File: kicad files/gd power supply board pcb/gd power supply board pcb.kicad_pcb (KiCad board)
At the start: 2 copper layers, 166.1 x 47.2 mm, 114 parts, among them J1 15V_IN, J2 15V_IN, J3 Edge Connector, Q1 FDS9435A, Q2 BC817, Q3 MMBT3906, Q4 FDS9435A, U1 MAX17580, U2 mc34063, U3 TPS563240DDCR, U4 TPS563240DDCR

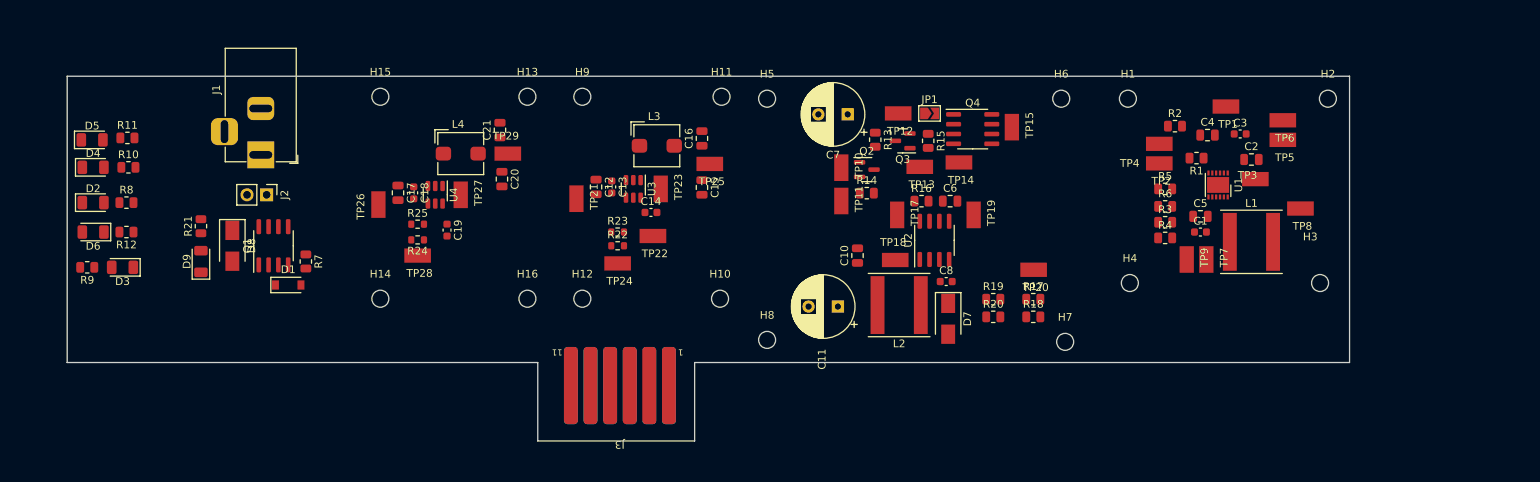
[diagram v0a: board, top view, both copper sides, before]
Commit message: minor fixes and compacting the floorplan. stacked 5V supplies for maximum minimage.
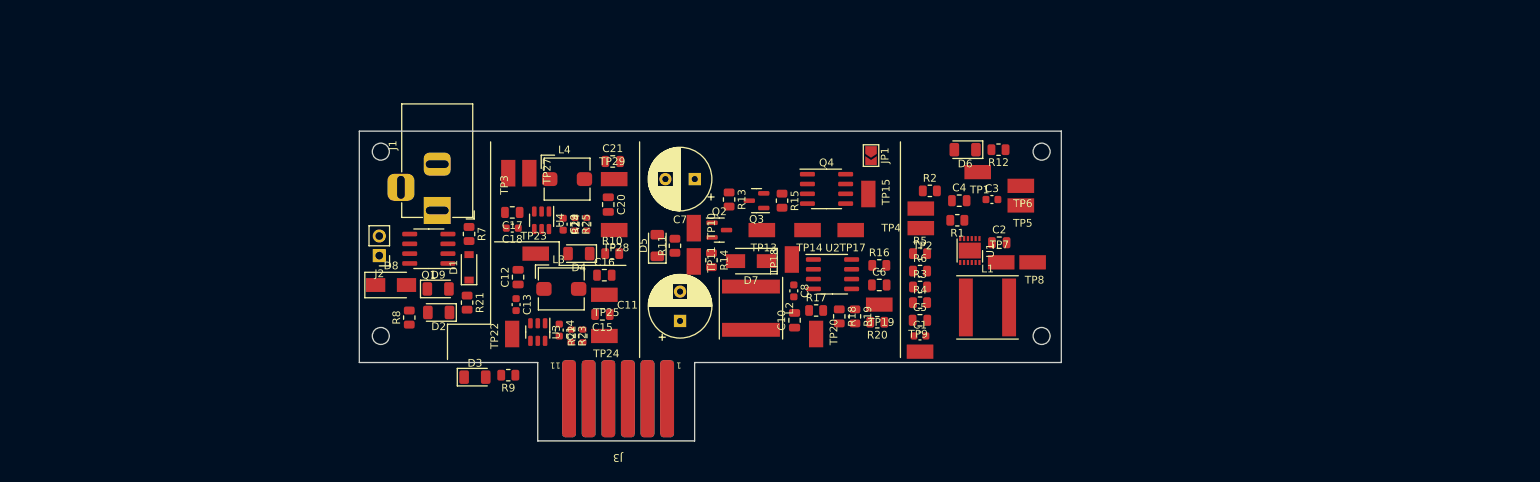
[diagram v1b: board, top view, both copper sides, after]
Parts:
- removed H10, H11, H12, H13, H14, H15, H16, H5, H6, H7, H8, H9: MountingHole, MountingHole:MountingHole_2.2mm_M2
- removed TP12, TP21, TP26: TestPoint_Harwin, My Libraries:Harwin-S1751-46-Test-Point
- moved R12 113.5 mm to (182.4, 81.3)
- moved D6 113.5 mm to (178.1, 81.3)
- moved H4 97.3 mm to (102.4, 105.4)
- moved H1 97.0 mm to (102.4, 81.5)
- moved TP3 96.8 mm to (118.9, 84.3), turned to 90 degrees
- moved D5 74.5 mm to (138.2, 93.7), turned to 90 degrees
- moved R11 72.3 mm to (140.5, 93.7), turned to 90 degrees
- moved D4 63.9 mm to (128.0, 94.7), turned to 180 degrees
- moved R10 63.7 mm to (132.3, 94.7)
- moved R9 56.3 mm to (118.9, 110.5)
- moved D3 47.8 mm to (114.6, 110.7), turned to 0 degrees
- moved D2 47.0 mm to (109.9, 102.4), turned to 180 degrees
- moved R8 39.5 mm to (106.0, 103.0), turned to 90 degrees
- moved C1 38.7 mm to (172.2, 105.4)
- moved C5 38.7 mm to (172.2, 103.4)
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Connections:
- R8 pad 2: /15v_In -> /15v_Raw
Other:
- board size 166.1 x 47.2 mm -> 90.9 x 40.1 mm

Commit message: pre-routing try 1
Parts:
- removed R4: 0, Resistor_SMD:R_0805_2012Metric
- removed R6: 1k, Resistor_SMD:R_0805_2012Metric
- removed TP1, TP2, TP4: TestPoint_Harwin, My Libraries:Harwin-S1751-46-Test-Point
- added C9: 1u, Capacitor_SMD:C_0805_2012Metric, B.Cu at (178.3, 92.4)
- added JP2: 15V_byp, Jumper:SolderJumper-2_P1.3mm_Open_TrianglePad1.0x1.5mm, F.Cu at (114.8, 100.6)
- added JP3: neg_12_jmp, Jumper:SolderJumper-2_P1.3mm_Open_TrianglePad1.0x1.5mm, F.Cu at (179.7, 81.0)
- added JP4: mega_5v_jmp, Jumper:SolderJumper-2_P1.3mm_Open_TrianglePad1.0x1.5mm, F.Cu at (118.1, 98.9)
- added JP5: stb_5v_jmp, Jumper:SolderJumper-2_P1.3mm_Open_TrianglePad1.0x1.5mm, F.Cu at (118.4, 82.2)
- C4: footprint Capacitor_SMD:C_0805_2012Metric -> Capacitor_SMD:C_0603_1608Metric
- R1: footprint Resistor_SMD:R_0805_2012Metric -> Resistor_SMD:R_0402_1005Metric
- TP5, TP6, TP8: footprint My Libraries:Harwin-S1751-46-Test-Point -> TestPoint:TestPoint_Pad_1.0x1.0mm
- moved R12 26.5 mm to (175.4, 106.9), turned to 90 degrees
- moved D6 26.1 mm to (179.0, 107.4), turned to 0 degrees
- moved C7 19.9 mm to (162.9, 84.3), turned to -90 degrees
- moved C1 19.2 mm to (176.7, 86.8), turned to 180 degrees
- moved TP20 18.8 mm to (143.4, 94.3)
- moved TP8 15.4 mm to (171.9, 92.2)
- moved TP14 15.0 mm to (144.2, 85.0), turned to 90 degrees
- moved C5 11.4 mm to (180.9, 96.0), turned to 90 degrees
- moved J3 9.93 mm to (143.0, 118.6)
- moved TP5 9.64 mm to (177.1, 83.4), turned to 180 degrees
- moved C10 9.58 mm to (146.7, 100.9), turned to -90 degrees
- moved TP15 9.44 mm to (156.5, 84.3), turned to 180 degrees
- moved R14 8.89 mm to (140.2, 88.2), turned to 180 degrees
- moved R2 8.84 mm to (181.9, 89.4), turned to -90 degrees
- moved JP1 8.68 mm to (157.2, 81.2)
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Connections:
- C12 pad 1: /Vin -> Net-(C12-Pad1)
- C13 pad 1: /Vin -> Net-(C12-Pad1)
- C17 pad 1: /Vin -> /stb_5v/stb_Vin
- C18 pad 1: /Vin -> /stb_5v/stb_Vin
- C2 pad 1: /Vin -> /neg12/neg12_Vin
- J3 pad 5: /stb_5v -> /mega_5v
- J3 pad 7: /mega_5v -> /stb_5v
- R3 pad 2: Net-(R3-Pad2) -> /neg12/FB
- R5 pad 2: Net-(R5-Pad2) -> /Neg12_Out
- U1 pad 1: /Vin -> /neg12/neg12_Vin
- U3 pad 3: /Vin -> Net-(C12-Pad1)
- U4 pad 3: /Vin -> /stb_5v/stb_Vin
- U4 pad 5: /Vin -> /stb_5v/stb_Vin
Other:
- board size 90.9 x 40.1 mm -> 86.9 x 40.1 mm

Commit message: 0 unrouted - drc pass - need to clean silks
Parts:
- JP2: moved to B.Cu
- moved D6 12.7 mm to (185.2, 96.3), turned to 90 degrees
- moved JP2 11.9 mm to (114.6, 88.6), turned to 0 degrees
- moved R12 11.2 mm to (183.0, 98.6), turned to -90 degrees
- moved TP18 6.85 mm to (154.6, 92.4), turned to 0 degrees
- moved TP7 6.52 mm to (175.5, 104.0), turned to 180 degrees
- moved TP19 5.24 mm to (163.3, 105.5)
- moved C11 3.51 mm to (143.0, 100.8), turned to 180 degrees
- moved C9 2.95 mm to (177.1, 89.7), turned to 180 degrees
- moved C10 1.88 mm to (146.8, 102.7)
- moved C5 1.72 mm to (182.3, 95.0), turned to 180 degrees
- moved C7 1.39 mm to (162.6, 85.6), turned to 0 degrees
- moved R2 1.04 mm to (182.9, 89.4)
- moved TP6 1.04 mm to (185.0, 88.7)
- moved C13 0.89 mm to (119.9, 101.4), turned to 180 degrees
- moved R20 0.81 mm to (164.3, 102.5)
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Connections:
- J3 pad 11: /Analog_En -> /Mega_En
- J3 pad 12: /Mega_En -> /Analog_En
- J3 pad 5: /mega_5v -> /stb_5v
- J3 pad 7: /stb_5v -> /mega_5v
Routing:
- net /Analog_En: track 0.00 -> 179.7 mm, vias 0 -> 4
- net /Mega_En: track 0.00 -> 29.3 mm, vias 0 -> 2
- net /mega_5v: track 0.00 -> 20.5 mm, vias 0 -> 2
- net Net-(R18-Pad1): track 0.00 -> 13.7 mm, vias 0 -> 2
- net Net-(R24-Pad1): track 0.00 -> 7.42 mm
- net /neg12/~{RESET}: track 0.00 -> 6.92 mm
- net /Pos12_Out: track 0.00 -> 6.64 mm
- net Net-(C8-Pad1): track 0.00 -> 4.86 mm
- net Net-(C3-Pad1): track 0.00 -> 4.11 mm
- net /stb_5v/stb_Vin: track 0.00 -> 3.76 mm, vias 0 -> 2
- net GND: track 0.00 -> 3.06 mm, vias 0 -> 32
- net Net-(D3-Pad2): track 0.00 -> 2.85 mm
- net Net-(R19-Pad2): track 0.00 -> 2.84 mm
- net Net-(C4-Pad1): track 0.00 -> 2.55 mm
- net Net-(D5-Pad2): track 0.00 -> 2.45 mm
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- added copper zone on B.Cu, net /15v_Raw
- added copper zone on F.Cu, net /15v_Raw
- added copper zone on F.Cu, net /Neg12_Out
- added copper zone on F.Cu, net /Pos12_Out
- added copper zone on F.Cu, net /Vin
- added copper zone on F.Cu, net /mega_5v
- added copper zone on F.Cu, net /neg12/FB
- added copper zone on F.Cu, net /neg12/neg12_Vin
- added copper zone on F.Cu, net /pos12/15V_SW
- added copper zone on F.Cu, net /pos12/Isense
- added copper zone on F.Cu, net /pos12/SW
- added copper zone on F.Cu, net /stb_5v
- added copper zone on F.Cu, net /stb_5v/stb_Vin
- added copper zone on B.Cu, net GND
- added copper zone on F.Cu, net GND
- added copper zone on F.Cu, net Net-(C12-Pad1)
- added copper zone on B.Cu, net Net-(C14-Pad1)
- added copper zone on F.Cu, net Net-(C14-Pad1)
- added copper zone on F.Cu, net Net-(C14-Pad2)
- added copper zone on B.Cu, net Net-(C19-Pad1)
- added copper zone on F.Cu, net Net-(C19-Pad1)
- added copper zone on F.Cu, net Net-(C19-Pad2)
- added copper zone on F.Cu, net Net-(C4-Pad2)
- added copper zone on F.Cu, net Net-(D1-Pad2)
- added copper zone on F.Cu, net Net-(D2-Pad2)
- added copper zone on F.Cu, net Net-(D8-Pad2)
- added copper zone on F.Cu, net Net-(D9-Pad2)
- added copper zone on F.Cu, net Net-(Q2-Pad2)
- added copper zone on F.Cu, net Net-(Q2-Pad3)
- added copper zone on F.Cu, net Net-(Q3-Pad1)
- added copper zone on F.Cu, net Net-(R22-Pad1)
- added copper zone on F.Cu, net Net-(R24-Pad1)
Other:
- outline, holes or cut-outs redrawn

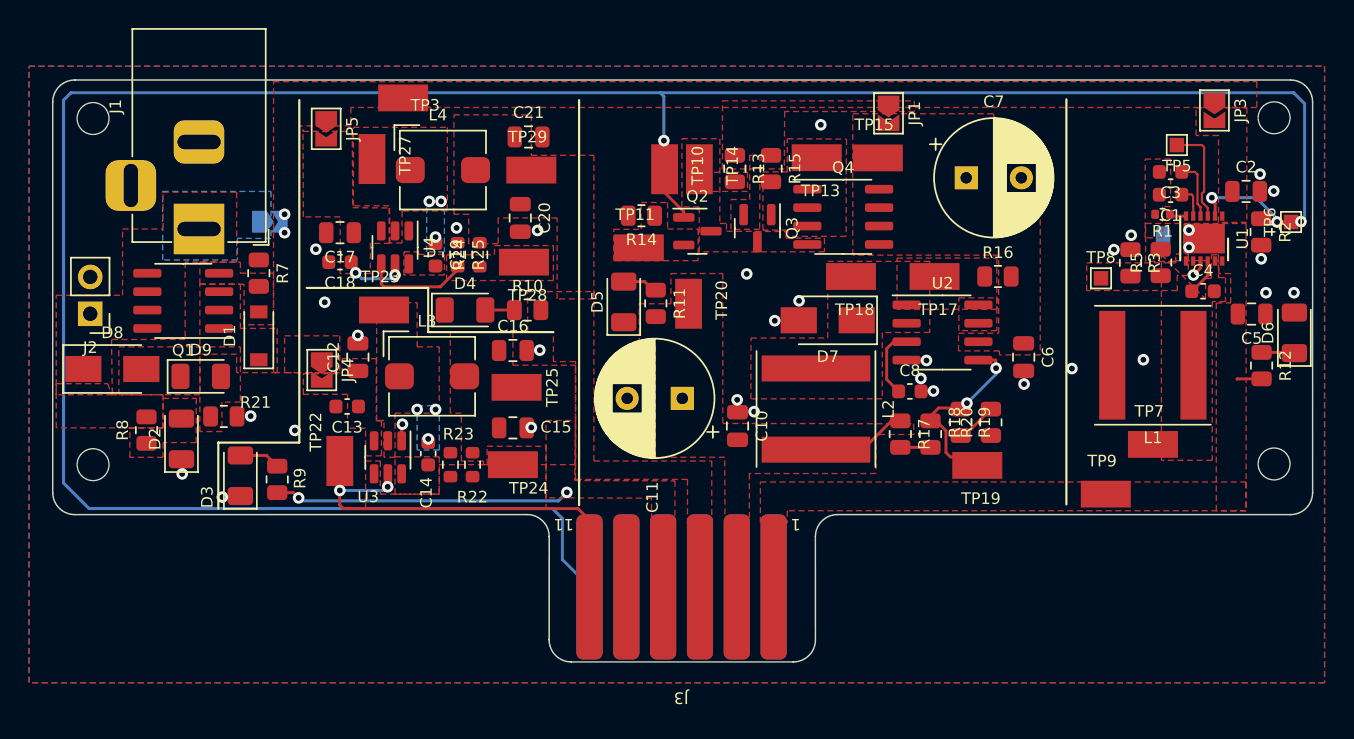
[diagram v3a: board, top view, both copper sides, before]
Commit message: cleaned up silks. minor fixes
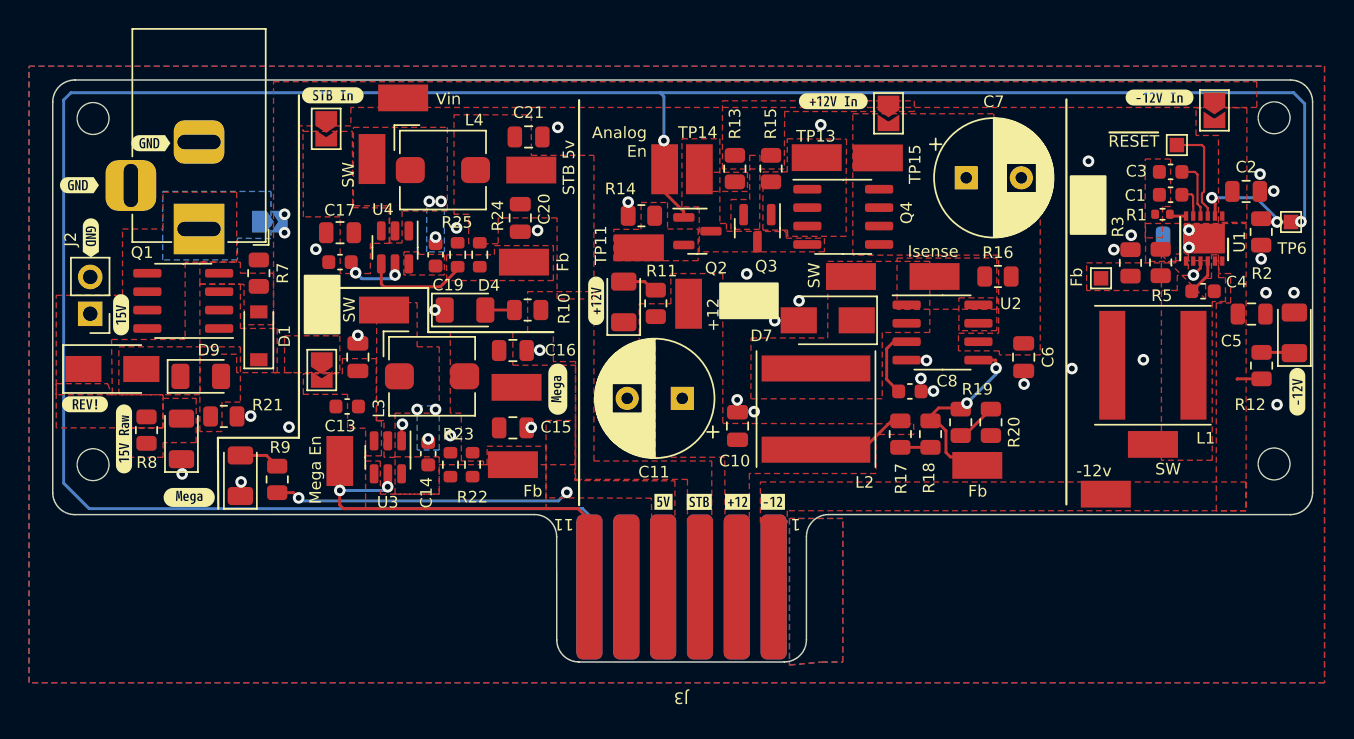
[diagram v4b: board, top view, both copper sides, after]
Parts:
- added TP1: TestPoint_Harwin, My Libraries:Harwin-S1751-46-Test-Point, F.Cu at (171.0, 87.5)
- added TP2: TestPoint_Harwin, My Libraries:Harwin-S1751-46-Test-Point, F.Cu at (118.2, 94.3)
- added TP4: TestPoint_Harwin, My Libraries:Harwin-S1751-46-Test-Point, F.Cu at (147.7, 94.0)
- added kibuzzard-62380C70: G***, kibuzzard-62380C70, F.Cu at (104.5, 103.6)
- added kibuzzard-62380CC4: G***, kibuzzard-62380CC4, F.Cu at (101.8, 101.2)
- added kibuzzard-62380CD9: G***, kibuzzard-62380CD9, F.Cu at (109.0, 107.7)
- added kibuzzard-62380CD9: G***, kibuzzard-62380CD9, F.Cu at (134.4, 100.2)
- added kibuzzard-62380D7E: G***, kibuzzard-62380D7E, F.Cu at (118.9, 79.9)
- added kibuzzard-62380DAB: G***, kibuzzard-62380DAB, F.Cu at (104.3, 95.1)
- added kibuzzard-62380E7D: G***, kibuzzard-62380E7D, F.Cu at (137.1, 94.1)
- added kibuzzard-62380F2D: G***, kibuzzard-62380F2D, F.Cu at (153.4, 80.3)
- added kibuzzard-62380F77: G***, kibuzzard-62380F77, F.Cu at (185.4, 100.4)
- added kibuzzard-62380FA1: G***, kibuzzard-62380FA1, F.Cu at (175.9, 80.1)
- added kibuzzard-62380FF5: G***, kibuzzard-62380FF5, F.Cu at (141.7, 108.0)
- added kibuzzard-62380FF5: G***, kibuzzard-62380FF5, B.Cu at (141.7, 108.0)
- added kibuzzard-62381000: G***, kibuzzard-62381000, F.Cu at (146.8, 108.0)
- added kibuzzard-62381000: G***, kibuzzard-62381000, B.Cu at (146.8, 108.0)
- added kibuzzard-6238101E: G***, kibuzzard-6238101E, F.Cu at (149.3, 108.0)
- added kibuzzard-6238101E: G***, kibuzzard-6238101E, B.Cu at (149.3, 108.0)
- added kibuzzard-62381032: G***, kibuzzard-62381032, F.Cu at (144.2, 108.0)
- added kibuzzard-62381032: G***, kibuzzard-62381032, B.Cu at (144.2, 108.0)
- added kibuzzard-6238106E: G***, kibuzzard-6238106E, F.Cu at (102.2, 89.8)
- added kibuzzard-6238106E: G***, kibuzzard-6238106E, F.Cu at (106.3, 83.2)
- added kibuzzard-6238106E: G***, kibuzzard-6238106E, F.Cu at (101.4, 86.1)
- added kibuzzard-6238106E: G***, kibuzzard-6238106E, B.Cu at (101.4, 86.1)
- added kibuzzard-6238106E: G***, kibuzzard-6238106E, B.Cu at (102.2, 90.2)
- added kibuzzard-6238106E: G***, kibuzzard-6238106E, B.Cu at (166.4, 87.9)
- added kibuzzard-6238106E: G***, kibuzzard-6238106E, B.Cu at (139.2, 103.1)
- added kibuzzard-6238106E: G***, kibuzzard-6238106E, B.Cu at (112.8, 83.1)
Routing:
- net /Analog_En: track 179.7 -> 181.0 mm
- net GND: vias 32 -> 38
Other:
- outline, holes or cut-outs redrawn
- board text added: "+12"
- board text added: "-12v"
- board text added: "Analog En"
- board text added: "Fb"
- board text added: "Isense"
- board text added: "Mega En"
- board text added: "STB 5v"
- board text added: "SW"
- board text added: "Vin"
- board text added: "~{RESET}"

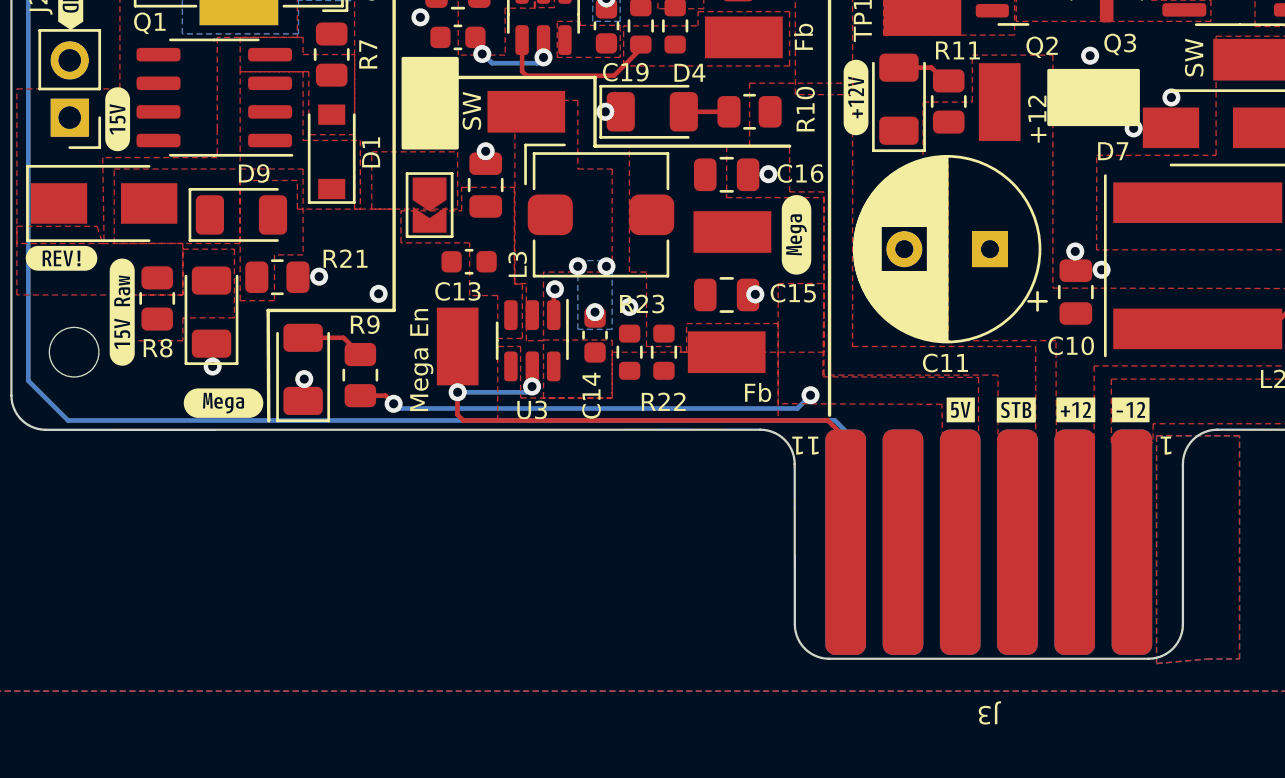
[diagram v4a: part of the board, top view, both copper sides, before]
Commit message: added a key/finger on the unused pads. also added polygon to ensure no mask on the edge connector
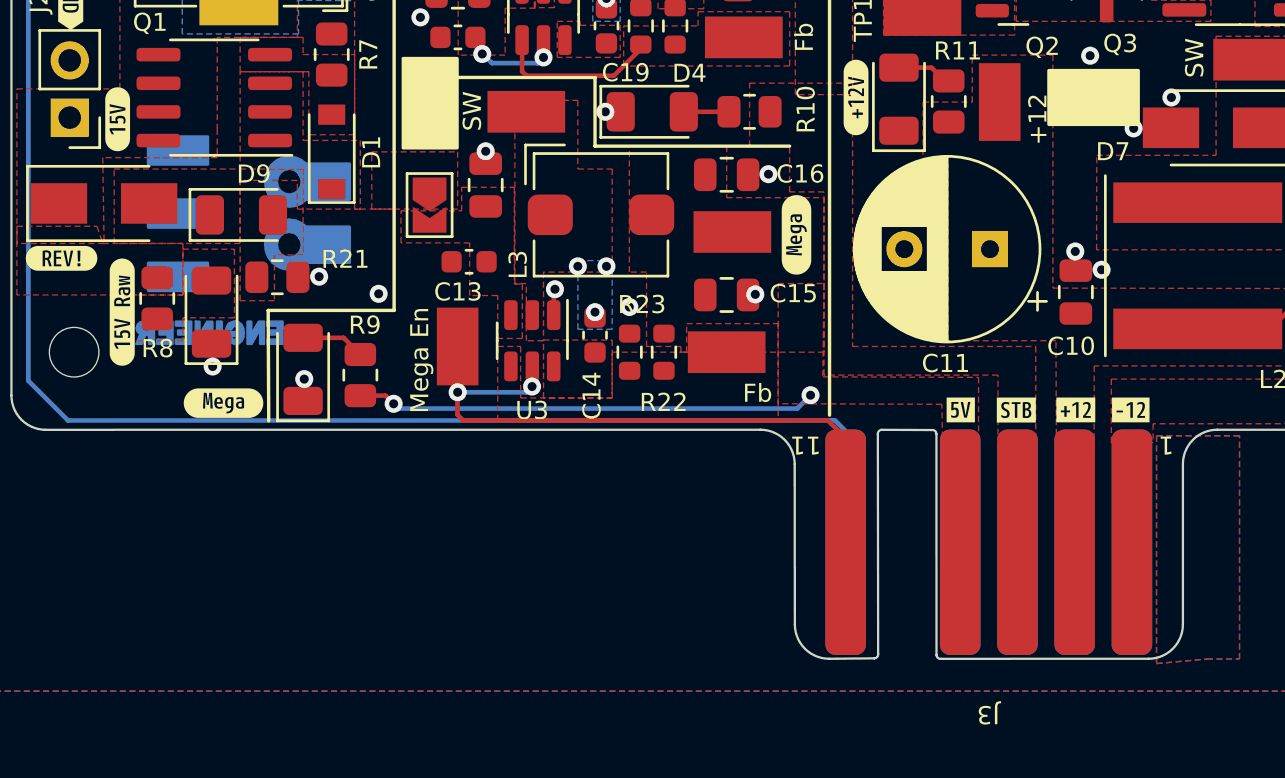
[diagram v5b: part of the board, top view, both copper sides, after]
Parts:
- added REF**: OSHW-Logo2_7.3x6mm_SilkScreen, Symbol:OSHW-Logo2_7.3x6mm_SilkScreen, B.Cu at (177.3, 104.2)
- added REF**: KiCad-Logo2_5mm_SilkScreen, Symbol:KiCad-Logo2_5mm_SilkScreen, B.Cu at (128.2, 97.9)
- added kibuzzard-62388B6B: G***, kibuzzard-62388B6B, B.Cu at (151.3, 87.5)
- added svg2mod: G***, My Libraries:BE10v2, B.Cu at (115.1, 95.1)
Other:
- outline, holes or cut-outs redrawn

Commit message: working on adapter board
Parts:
- removed the kibuzzard-62380FF5 at (141.7, 108.0)
- removed the kibuzzard-62381000 at (146.8, 108.0)
- removed the kibuzzard-6238101E at (149.3, 108.0)
- removed the kibuzzard-62381032 at (144.2, 108.0)
- added REF**: Polarity_Center_Positive_6mm_SilkScreen, Symbol:Polarity_Center_Positive_6mm_SilkScreen, B.Cu at (129.1, 83.5)
- moved kibuzzard-62388B6B 13.2 mm to (163.1, 93.5)
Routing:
- net /Analog_En: track 181.0 -> 180.4 mm
- net GND: vias 38 -> 39
